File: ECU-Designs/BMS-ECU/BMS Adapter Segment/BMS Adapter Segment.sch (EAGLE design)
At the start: 61 parts, among them X1 CONNECTOR-10NANO-FIT_VERTICAL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, X10 CONNECTOR-2NANO-FIT_VERTICAL_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, X11 CONNECTOR-2NANO-FIT_VERTICAL_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, X12 CONNECTOR-2NANO-FIT_VERTICAL_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, X13 CONNECTOR-10NANO-FIT_VERTICAL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, X2 CONNECTOR-2NANO-FIT_VERTICAL_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, X3 CONNECTOR-2NANO-FIT_VERTICAL_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, X5 CONNECTOR-4NANO-FIT_VERTICAL_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, X6 CONNECTOR-4NANO-FIT_VERTICAL_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, X7 CONNECTOR-2NANO-FIT_VERTICAL_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, X8 CONNECTOR-2NANO-FIT_VERTICAL_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, X9 CONNECTOR-2NANO-FIT_VERTICAL_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

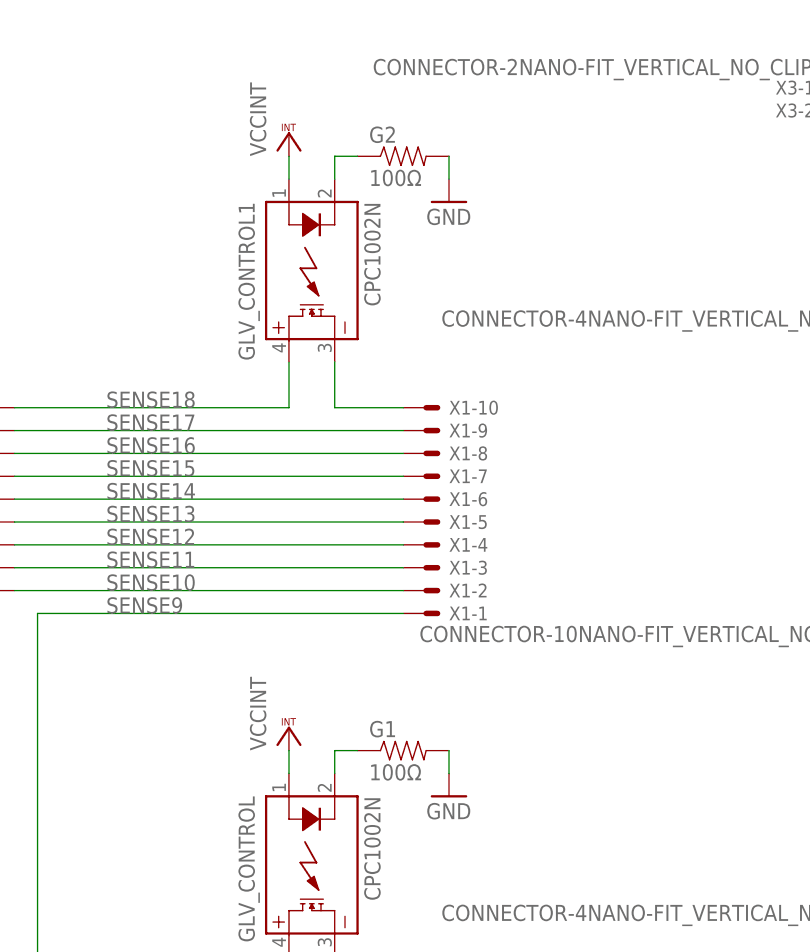
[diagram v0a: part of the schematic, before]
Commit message: Changed BMS SSR control resistors to 2K resistors
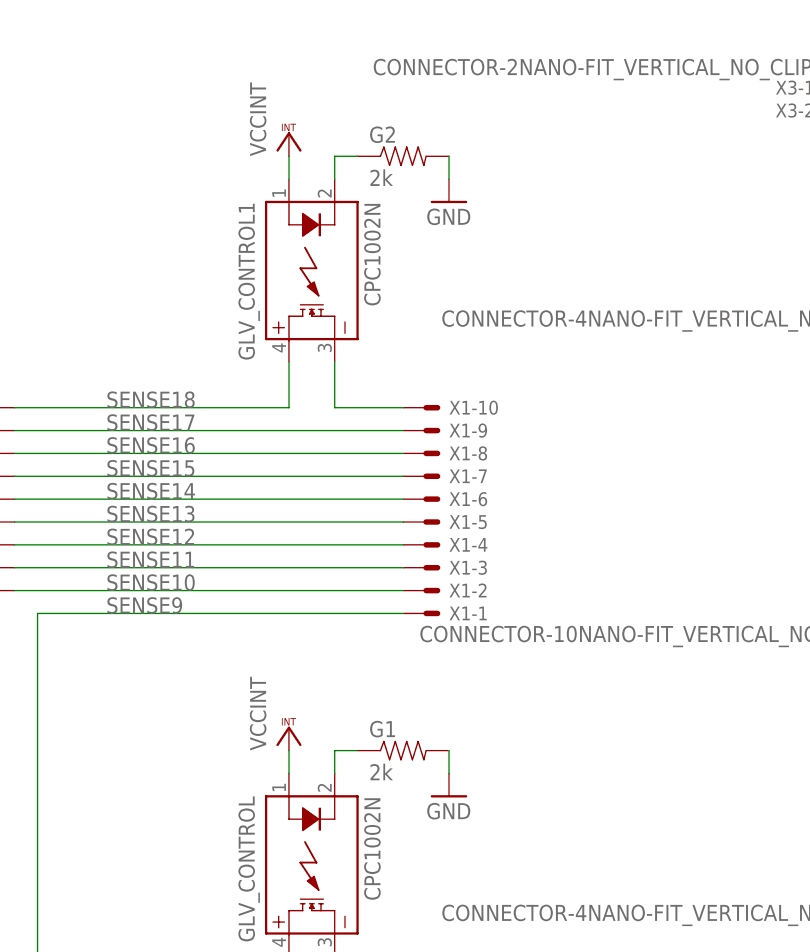
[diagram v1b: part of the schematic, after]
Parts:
- G1, G2: value 100Ω -> 2k
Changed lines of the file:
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@@
 <grid distance="0.1" unitdist="inch" unit="inch" style="lines" multiple="1" display="no" altdistance="0.01" altunitdist="inch" altunit="inch"/>
 <layers>
-<layer number="1" name="Top" color="4" fill="1" visible="yes" active="no"/>
-<layer number="2" name="Route2" color="1" fill="3" visible="yes" active="no"/>
-<layer number="3" name="Route3" color="4" fill="3" visible="yes" active="no"/>
-<layer number="4" name="Route4" color="1" fill="4" visible="yes" active="no"/>
-<layer number="5" name="Route5" color="4" fill="4" visible="yes" active="no"/>
-<layer number="6" name="Route6" color="1" fill="8" visible="yes" active="no"/>
-<layer number="7" name="Route7" color="4" fill="8" visible="yes" active="no"/>
-<layer number="8" name="Route8" color="1" fill="2" visible="yes" active="no"/>
-<layer number="9" name="Route9" color="4" fill="2" visible="yes" active="no"/>
-<layer number="10" name="Route10" color="1" fill="7" visible="yes" active="no"/>
-<layer number="11" name="Route11" color="4" fill="7" visible="yes" active="no"/>
-<layer number="12" name="Route12" color="1" fill="5" visible="yes" active="no"/>
-<layer number="13" name="Route13" color="4" fill="5" visible="yes" active="no"/>
-<layer number="14" name="Route14" color="1" fill="6" visible="yes" active="no"/>
-<layer number="15" name="Route15" color="4" fill="6" visible="yes" active="no"/>
-<layer number="16" name="Bottom" color="1" fill="1" visible="yes" active="no"/>
-<layer number="17" name="Pads" color="2" fill="1" visible="yes" active="no"/>
-<layer number="18" name="Vias" color="2" fill="1" visible="yes" active="no"/>
-<layer number="19" name="Unrouted" color="6" fill="1" visible="yes" active="no"/>
-<layer number="20" name="Dimension" color="15" fill="1" visible="yes" active="no"/>
-<layer number="21" name="tPlace" color="7" fill="1" visible="yes" active="no"/>
-<layer number="22" name="bPlace" color="7" fill="1" visible="yes" active="no"/>
-<layer number="23" name="tOrigins" color="15" fill="1" visible="yes" active="no"/>
-<layer number="24" name="bOrigins" color="15" fill="1" visible="yes" active="no"/>
-<layer number="25" name="tNames" color="7" fill="1" visible="yes" active="no"/>
-<layer number="26" name="bNames" color="7" fill="1" visible="yes" active="no"/>
-<layer number="27" name="tValues" color="7" fill="1" visible="yes" active="no"/>
-<layer number="28" name="bValues" color="7" fill="1" visible="yes" active="no"/>
+<layer number="1" name="Top" color="4" fill="1" visible="no" active="no"/>
+<layer number="2" name="Route2" color="1" fill="3" visible="no" active="no"/>
+<layer number="3" name="Route3" color="4" fill="3" visible="no" active="no"/>
+<layer number="4" name="Route4" color="1" fill="4" visible="no" active="no"/>
+<layer number="5" name="Route5" color="4" fill="4" visible="no" active="no"/>
+<layer number="6" name="Route6" color="1" fill="8" visible="no" active="no"/>
+<layer number="7" name="Route7" color="4" fill="8" visible="no" active="no"/>
+<layer number="8" name="Route8" color="1" fill="2" visible="no" active="no"/>
+<layer number="9" name="Route9" color="4" fill="2" visible="no" active="no"/>
+<layer number="10" name="Route10" color="1" fill="7" visible="no" active="no"/>
+<layer number="11" name="Route11" color="4" fill="7" visible="no" active="no"/>
+<layer number="12" name="Route12" color="1" fill="5" visible="no" active="no"/>
+<layer number="13" name="Route13" color="4" fill="5" visible="no" active="no"/>
+<layer number="14" name="Route14" color="1" fill="6" visible="no" active="no"/>
+<layer number="15" name="Route15" color="4" fill="6" visible="no" active="no"/>
+<layer number="16" name="Bottom" color="1" fill="1" visible="no" active="no"/>
+<layer number="17" name="Pads" color="2" fill="1" visible="no" active="no"/>
+<layer number="18" name="Vias" color="2" fill="1" visible="no" active="no"/>
+<layer number="19" name="Unrouted" color="6" fill="1" visible="no" active="no"/>
+<layer number="20" name="Dimension" color="15" fill="1" visible="no" active="no"/>
+<layer number="21" name="tPlace" color="7" fill="1" visible="no" active="no"/>
+<layer number="22" name="bPlace" color="7" fill="1" visible="no" active="no"/>
+<layer number="23" name="tOrigins" color="15" fill="1" visible="no" active="no"/>
+<layer number="24" name="bOrigins" color="15" fill="1" visible="no" active="no"/>
+<layer number="25" name="tNames" color="7" fill="1" visible="no" active="no"/>
+<layer number="26" name="bNames" color="7" fill="1" visible="no" active="no"/>
+<layer number="27" name="tValues" color="7" fill="1" visible="no" active="no"/>
+<layer number="28" name="bValues" color="7" fill="1" visible="no" active="no"/>
 <layer number="29" name="tStop" color="7" fill="3" visible="no" active="no"/>
 <layer number="30" name="bStop" color="7" fill="6" visible="no" active="no"/>
@@
 <layer number="35" name="tGlue" color="7" fill="4" visible="no" active="no"/>
 <layer number="36" name="bGlue" color="7" fill="5" visible="no" active="no"/>
-<layer number="37" name="tTest" color="7" fill="1" visible="yes" active="no"/>
-<layer number="38" name="bTest" color="7" fill="1" visible="yes" active="no"/>
+<layer number="37" name="tTest" color="7" fill="1" visible="no" active="no"/>
+<layer number="38" name="bTest" color="7" fill="1" visible="no" active="no"/>
 <layer number="39" name="tKeepout" color="4" fill="11" visible="no" active="no"/>
 <layer number="40" name="bKeepout" color="1" fill="11" visible="no" active="no"/>
@@
 <layer number="44" name="Drills" color="7" fill="1" visible="no" active="no"/>
 <layer number="45" name="Holes" color="7" fill="1" visible="no" active="no"/>
-<layer number="46" name="Milling" color="3" fill="1" visible="yes" active="no"/>
-<layer number="47" name="Measures" color="7" fill="1" visible="yes" active="no"/>
-<layer number="48" name="Document" color="7" fill="1" visible="yes" active="no"/>
-<layer number="49" name="Reference" color="7" fill="1" visible="yes" active="no"/>
-<layer number="50" name="dxf" color="7" fill="1" visible="yes" active="no"/>
-<layer number="51" name="tDocu" color="7" fill="1" visible="yes" active="no"/>
-<layer number="52" name="bDocu" color="7" fill="1" visible="yes" active="no"/>
-<layer number="53" name="tGND_GNDA" color="7" fill="9" visible="yes" active="no"/>
-<layer number="54" name="bGND_GNDA" color="1" fill="9" visible="yes" active="no"/>
-<layer number="56" name="wert" color="7" fill="1" visible="yes" active="no"/>
-<layer number="57" name="tCAD" color="7" fill="1" visible="yes" active="no"/>
-<layer number="59" name="tCarbon" color="7" fill="1" visible="yes" active="no"/>
-<layer number="60" name="bCarbon" color="7" fill="1" visible="yes" active="no"/>
+<layer number="46" name="Milling" color="3" fill="1" visible="no" active="no"/>
+<layer number="47" name="Measures" color="7" fill="1" visible="no" active="no"/>
+<layer number="48" name="Document" color="7" fill="1" visible="no" active="no"/>
+<layer number="49" name="Reference" color="7" fill="1" visible="no" active="no"/>
+<layer number="50" name="dxf" color="7" fill="1" visible="no" active="no"/>
+<layer number="51" name="tDocu" color="7" fill="1" visible="no" active="no"/>
+<layer number="52" name="bDocu" color="7" fill="1" visible="no" active="no"/>
+<layer number="53" name="tGND_GNDA" color="7" fill="9" visible="no" active="no"/>
+<layer number="54" name="bGND_GNDA" color="1" fill="9" visible="no" active="no"/>
+<layer number="56" name="wert" color="7" fill="1" visible="no" active="no"/>
+<layer number="57" name="tCAD" color="7" fill="1" visible="no" active="no"/>
+<layer number="59" name="tCarbon" color="7" fill="1" visible="no" active="no"/>
+<layer number="60" name="bCarbon" color="7" fill="1" visible="no" active="no"/>
 <layer number="90" name="Modules" color="5" fill="1" visible="yes" active="yes"/>
 <layer number="91" name="Nets" color="2" fill="1" visible="yes" active="yes"/>
@@
 <part name="GLV_CONTROL" library="HyTechDevices" deviceset="CPC1002N" device=""/>
 <part name="GND1" library="supply1" deviceset="GND" device=""/>
-<part name="G1" library="HyTechDevices" deviceset="RESISTOR" device="0805-RES" value="100Ω"/>
+<part name="G1" library="HyTechDevices" deviceset="RESISTOR" device="0805-RES" value="2k"/>
 <part name="F10" library="HyTechDevices" deviceset="0751.0110_FUSE_CLIP" device="" value=""/>
 <part name="F11" library="HyTechDevices" deviceset="0751.0110_FUSE_CLIP" device="" value=""/>
@@
 <part name="GLV_CONTROL1" library="HyTechDevices" deviceset="CPC1002N" device=""/>
 <part name="GND3" library="supply1" deviceset="GND" device=""/>
-<part name="G2" library="HyTechDevices" deviceset="RESISTOR" device="0805-RES" value="100Ω"/>
+<part name="G2" library="HyTechDevices" deviceset="RESISTOR" device="0805-RES" value="2k"/>
 <part name="VCC3" library="supply1" deviceset="VCCINT" device=""/>
 <part name="X6" library="HyTechDevices" deviceset="CONNECTOR-4" device="NANO-FIT_VERTICAL_NO_CLIPS-4" value="CONNECTOR-4NANO-FIT_VERTICAL_NO_CLIPS-4"/>
